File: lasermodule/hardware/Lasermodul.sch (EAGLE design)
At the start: 79 parts, among them IC1 MEGA8-AI

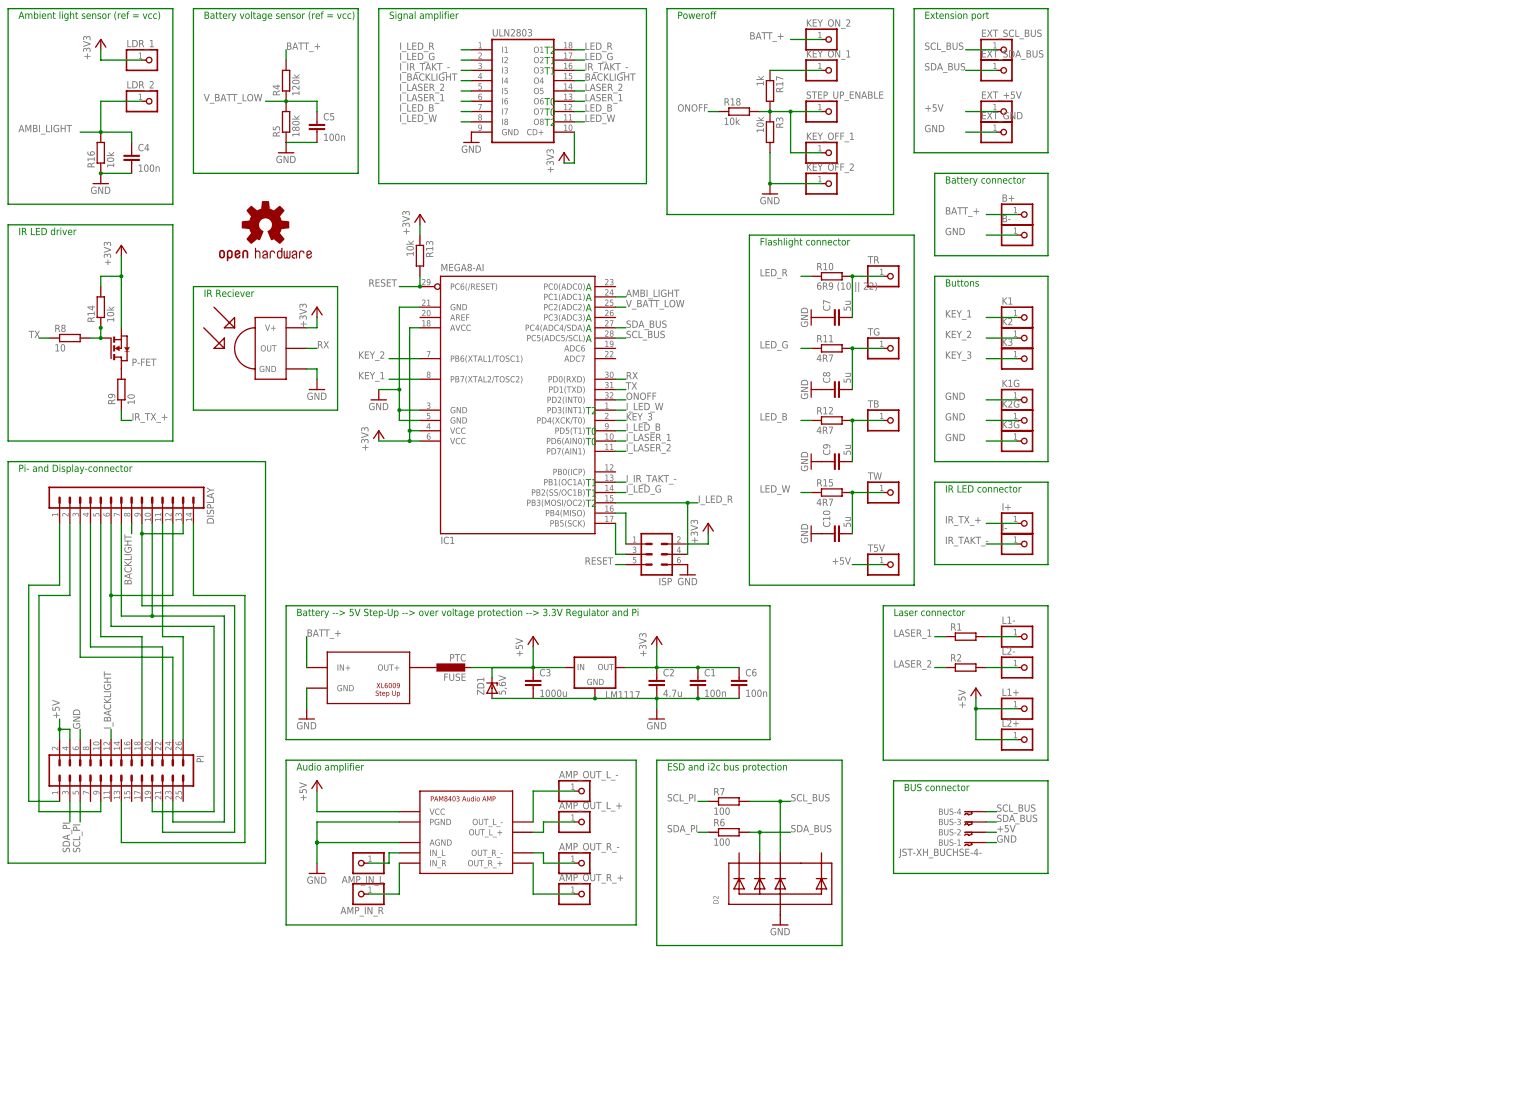
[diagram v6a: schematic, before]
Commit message: lasermodul: second ir led added (shotgun, sniper)
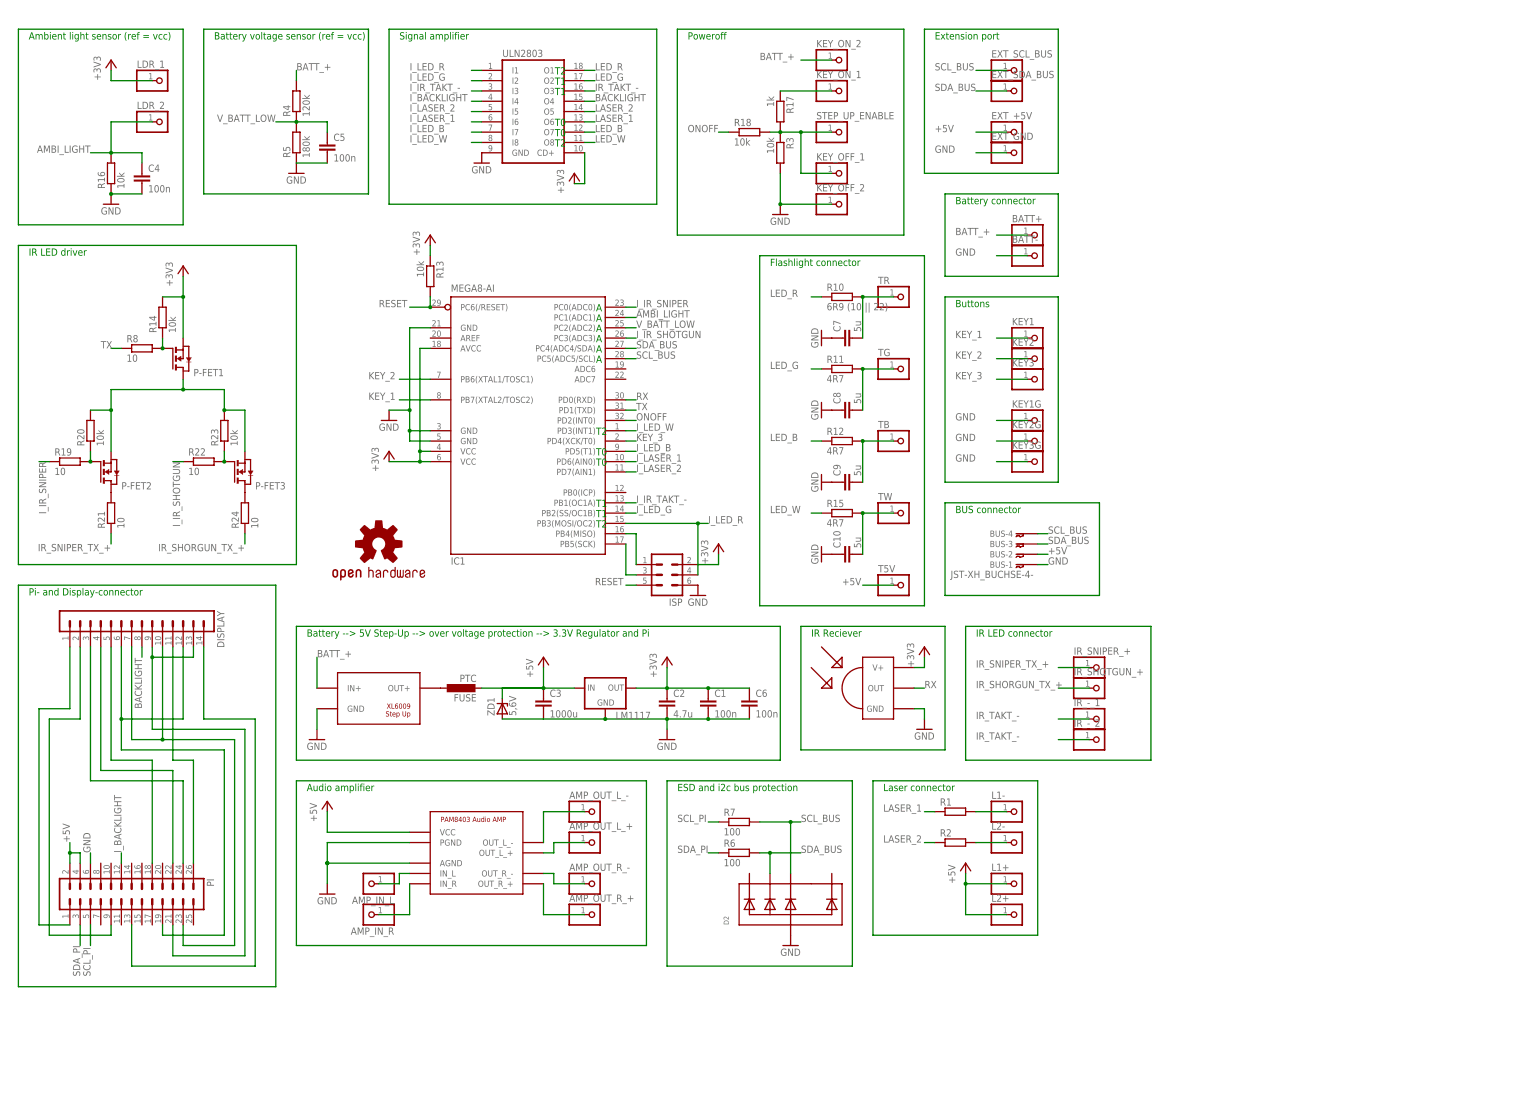
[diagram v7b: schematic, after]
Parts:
- removed B+, B-, I+, I-, K1, K1G, K2, K2G, K3, K3G: (no value), wz:PIN-HEADER-1
- removed P-FET: (no value), zetex:NMOSSOT23
- removed R9: 10, wz:R_EU0603
- added BATT+, BATT-, IR_-_1, IR_-_2, IR_SHOTGUN_+, IR_SNIPER_+, KEY1, KEY1G, KEY2, KEY2G, KEY3, KEY3G: (no value), wz:PIN-HEADER-1
- added P-FET1, P-FET2, P-FET3: (no value), zetex:NMOSSOT23
- added R19, R21, R22, R24: 10, wz:R_EU0603
- added R20, R23: 10k, wz:R_EU0603
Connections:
- removed net IR_TX_+: I+.1, R9.1
- removed net N$16: P-FET.D, R9.2
- new net +3V2: P-FET1.D, P-FET2.S, P-FET3.S, R20.2, R23.2
- new net IR_SHORGUN_TX_+: IR_SHOTGUN_+.1, R24.1
- new net IR_SNIPER_TX_+: IR_SNIPER_+.1, R21.1
- new net I_IR_SHOTGUN: IC1.PC3(ADC3), R22.1
- new net I_IR_SNIPER: IC1.PC0(ADC0), R19.1
- new net N$34: P-FET2.D, R21.2
- new net N$46: P-FET2.G, R19.2, R20.1
- new net N$53: P-FET3.D, R24.2
- new net N$54: P-FET3.G, R22.2, R23.1
- net +3V3: now also P-FET1.S; no longer P-FET.S
- net BATT_+: now also BATT+.1; no longer B+.1
- net GND: now also BATT-.1, KEY1G.1, KEY2G.1, KEY3G.1; no longer B-.1, K1G.1, K2G.1, K3G.1
- net IR_TAKT_-: now also IR_-_1.1, IR_-_2.1; no longer I-.1
- net KEY_1: now also KEY1.1; no longer K1.1
- net KEY_2: now also KEY2.1; no longer K2.1
- net KEY_3: now also KEY3.1; no longer K3.1
- net N$20: now also P-FET1.G; no longer P-FET.G
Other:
- moved on the sheet: AMP_IN_L, AMP_IN_R, AMP_OUT_L_+, AMP_OUT_L_-, AMP_OUT_R_+, AMP_OUT_R_-, BUS-1, BUS-2, BUS-3, BUS-4, C1, C10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

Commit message: Revert "lasermodul: second ir led added (shotgun, sniper)"
This reverts commit 9edbfcc3dcd4b30951dc51917cfd3b2c003d7d33.
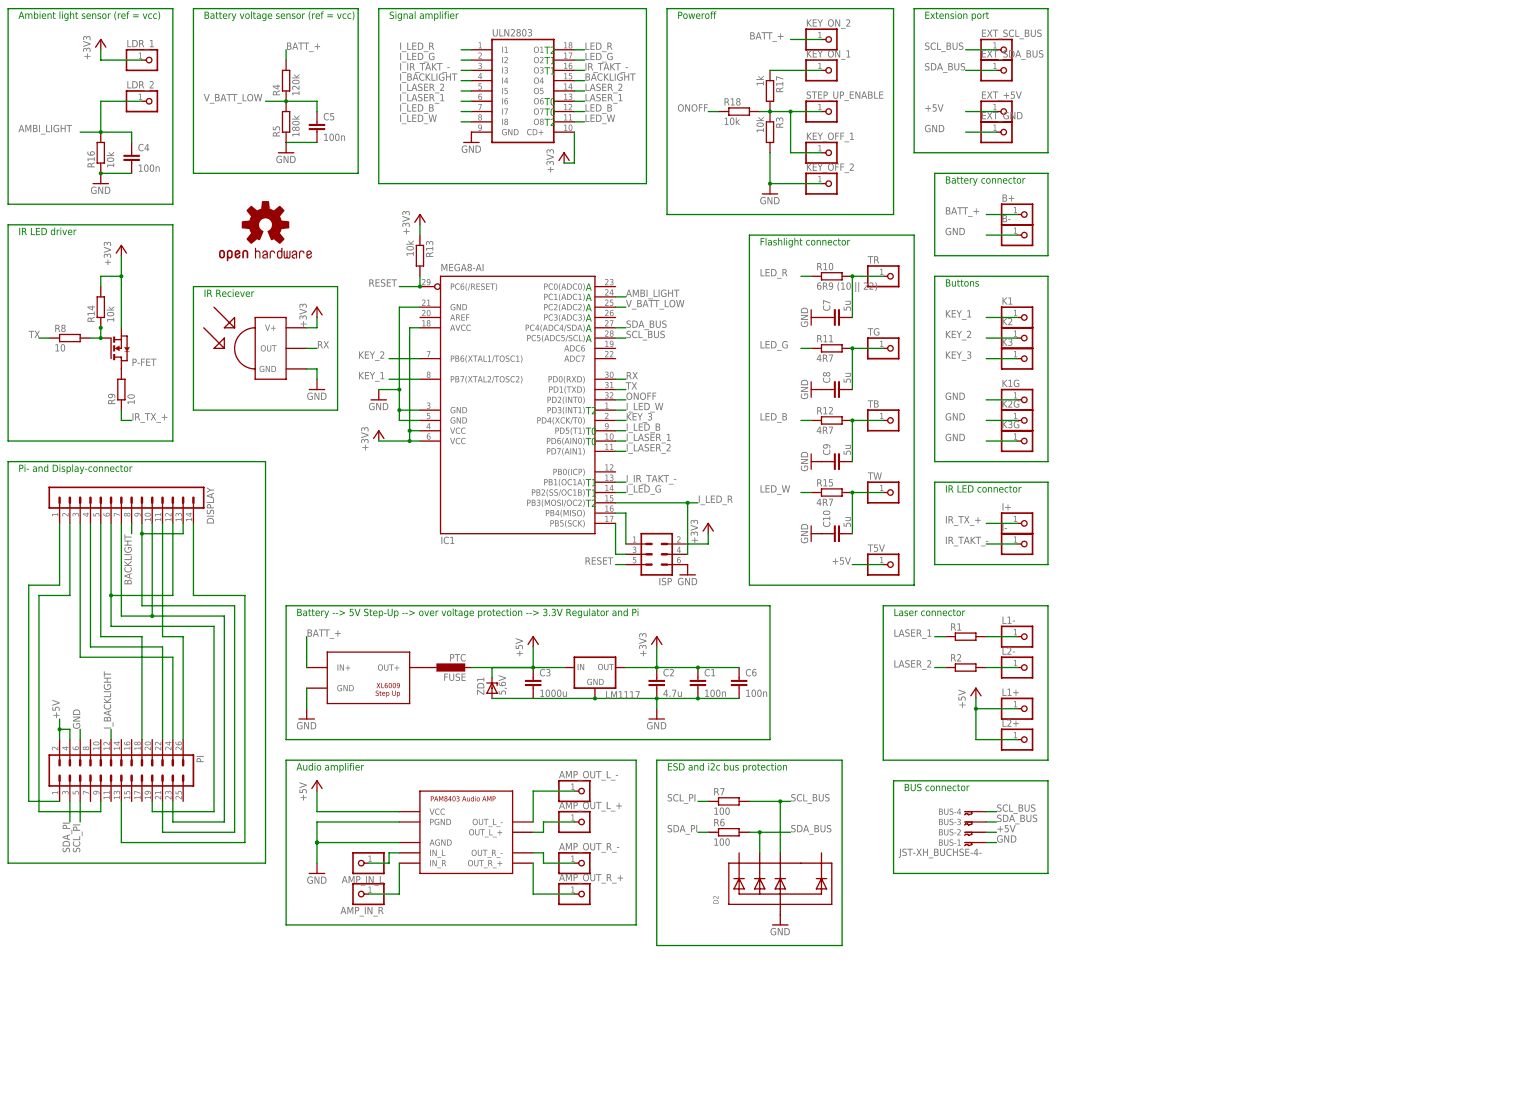
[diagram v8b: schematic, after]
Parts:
- removed BATT+, BATT-, IR_-_1, IR_-_2, IR_SHOTGUN_+, IR_SNIPER_+, KEY1, KEY1G, KEY2, KEY2G, KEY3, KEY3G: (no value), wz:PIN-HEADER-1
- removed P-FET1, P-FET2, P-FET3: (no value), zetex:NMOSSOT23
- removed R19, R21, R22, R24: 10, wz:R_EU0603
- removed R20, R23: 10k, wz:R_EU0603
- added B+, B-, I+, I-, K1, K1G, K2, K2G, K3, K3G: (no value), wz:PIN-HEADER-1
- added P-FET: (no value), zetex:NMOSSOT23
- added R9: 10, wz:R_EU0603
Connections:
- removed net +3V2: P-FET1.D, P-FET2.S, P-FET3.S, R20.2, R23.2
- removed net IR_SHORGUN_TX_+: IR_SHOTGUN_+.1, R24.1
- removed net IR_SNIPER_TX_+: IR_SNIPER_+.1, R21.1
- removed net I_IR_SHOTGUN: IC1.PC3(ADC3), R22.1
- removed net I_IR_SNIPER: IC1.PC0(ADC0), R19.1
- removed net N$34: P-FET2.D, R21.2
- removed net N$46: P-FET2.G, R19.2, R20.1
- removed net N$53: P-FET3.D, R24.2
- removed net N$54: P-FET3.G, R22.2, R23.1
- new net IR_TX_+: I+.1, R9.1
- new net N$16: P-FET.D, R9.2
- net +3V3: now also P-FET.S; no longer P-FET1.S
- net BATT_+: now also B+.1; no longer BATT+.1
- net GND: now also B-.1, K1G.1, K2G.1, K3G.1; no longer BATT-.1, KEY1G.1, KEY2G.1, KEY3G.1
- net IR_TAKT_-: now also I-.1; no longer IR_-_1.1, IR_-_2.1
- net KEY_1: now also K1.1; no longer KEY1.1
- net KEY_2: now also K2.1; no longer KEY2.1
- net KEY_3: now also K3.1; no longer KEY3.1
- net N$20: now also P-FET.G; no longer P-FET1.G
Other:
- moved on the sheet: AMP_IN_L, AMP_IN_R, AMP_OUT_L_+, AMP_OUT_L_-, AMP_OUT_R_+, AMP_OUT_R_-, BUS-1, BUS-2, BUS-3, BUS-4, C1, C10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
